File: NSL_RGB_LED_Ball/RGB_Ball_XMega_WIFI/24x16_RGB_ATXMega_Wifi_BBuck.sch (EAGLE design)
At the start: 107 parts, among them IC2 TLC5947XLP, IC3 TLC5947XLP, IC4 TLC5947XLP, IC5 MCP73123, IC6 CC3000, IC7 MMA7455L, IC8 OPA344, X1 NX3225GA-16.000M-STD-CRG-2

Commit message: 
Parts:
- removed BATTERY1: (no value), SparkFun:M02PTH
- added C26, C28, C30: 10uF, CH_passive:CAP0805
- added C27, C29: 0.1, CH_passive:CAP0805
- added L3: 2.2uH 1.6A, CH_passive:INDUCTOR1313
- added R16, R9: see notes, CH_passive:RESISTOR0805
- added R17: 100K, slice_noshift:RESISTOR0805
- added R7, R8: 1M, CH_passive:RESISTOR0805
- added U1: TPS6120x, CH_TI:TPS61200
- R6: value 220K -> 100K
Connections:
- new net +3V3: C1.1, C2.1, C20.2, C28.1, C30.1, C5.1, C6.1, C7.1, C8.1, IC1.AVCC, IC1.VCC@1, IC1.VCC@2, IC1.VCC@3, IC7.AVDD, IC7.DVDD_IO, IC8.V+, JP1.4, R11.2, R13.2, U1.FB, U1.VOUT, Z1.P$4
- new net EN: R7.1, U1.EN
- new net N$24: L3.2, U1.L
- new net N$30: C27.1, U1.VAUX
- new net PS: R8.1, U1.PS
- new net UVLO: C29.2, R16.2, R9.1, U1.UVLO
- net BATTSENSE: now also R17.2
- net GND: now also C26.2, C27.2, C28.2, C30.2, JP2.1, R16.1, R17.1, U1.GND, U1.PAD@1, U1.PAD@2, U1.PAD@3, U1.PAD@4, U1.PAD@5, U1.PGND; no longer BATTERY1.1, JP2.4, VCC.1
- net N$7: now also JP2.4; no longer JP2.1
- net VCC: now also C26.1, C29.1, L3.1, R7.2, R8.2, R9.2, U1.VIN, VCC.1; no longer BATTERY1.2, C1.1, C2.1, C20.2, C5.1, C6.1, C7.1, C8.1, IC1.AVCC, IC1.VCC@1, IC1.VCC@2, IC1.VCC@3, IC7.AVDD, IC7.DVDD_IO, IC8.V+, JP1.4, R11.2, R13.2, Z1.P$4
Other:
- note added: "GND, PGND connected w/non-current bearing trace"
- note added: "Notes:"
- note added: "R3 1330K, R4 249K"
- note added: "R3 2100K, R4 232K"
- note added: "R3 2150K, R4 249K"
- note added: "R3 549K, R4 249K"
- note added: "R3 953K,"
- note added: "R3, R4 1% film"
- note added: "R4 95.3K"
- note added: "Sumida CDRH2D18"
- note added: "UVLO 0.8V (Single NiMH)"
- note added: "UVLO 1.6V (Dual NiMH)"
- note added: "UVLO 2.4V (Triple NiMH)"
- note added: "UVLO 2.5V (LiPo)"
- note added: "UVLO 2.75V"
- note added: "UVLO 2.75V (LiPo)"
- note added: "same values can be used for 5V feedback divider"

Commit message: 
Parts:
- added C31: 12pF, SparkFun:CAP0805
- added C32: 1uF, 24x16_RGB:CAP0805
- added TP15: MIC, testpad:PTR1TP12SQ
- added TP16: BATT, testpad:PTR1TP12SQ
- C23: value .1uF -> 47uF; device SparkFun:CAP0805 -> slice_noshift:CAP_POL3528; MPN 08055C105MAT2A -> (none); OC_NEWARK 73T5385 -> unknown
- JP4: device SparkFun-Connectors:M041.27MM -> SparkFun-Connectors:M04PTH
- R1, R2, R3: value 47K -> 20K
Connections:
- net +3V3: now also C23.+, C31.1, C32.1
- net BATTSENSE: now also TP16.TP
- net GND: now also C23.-, C31.2, C32.2; no longer C23.2
- net MIC: now also TP15.TP
- net N$17: no longer C23.1
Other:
- note removed: "If making new board flip PWR and GND"
- moved on the sheet: C13

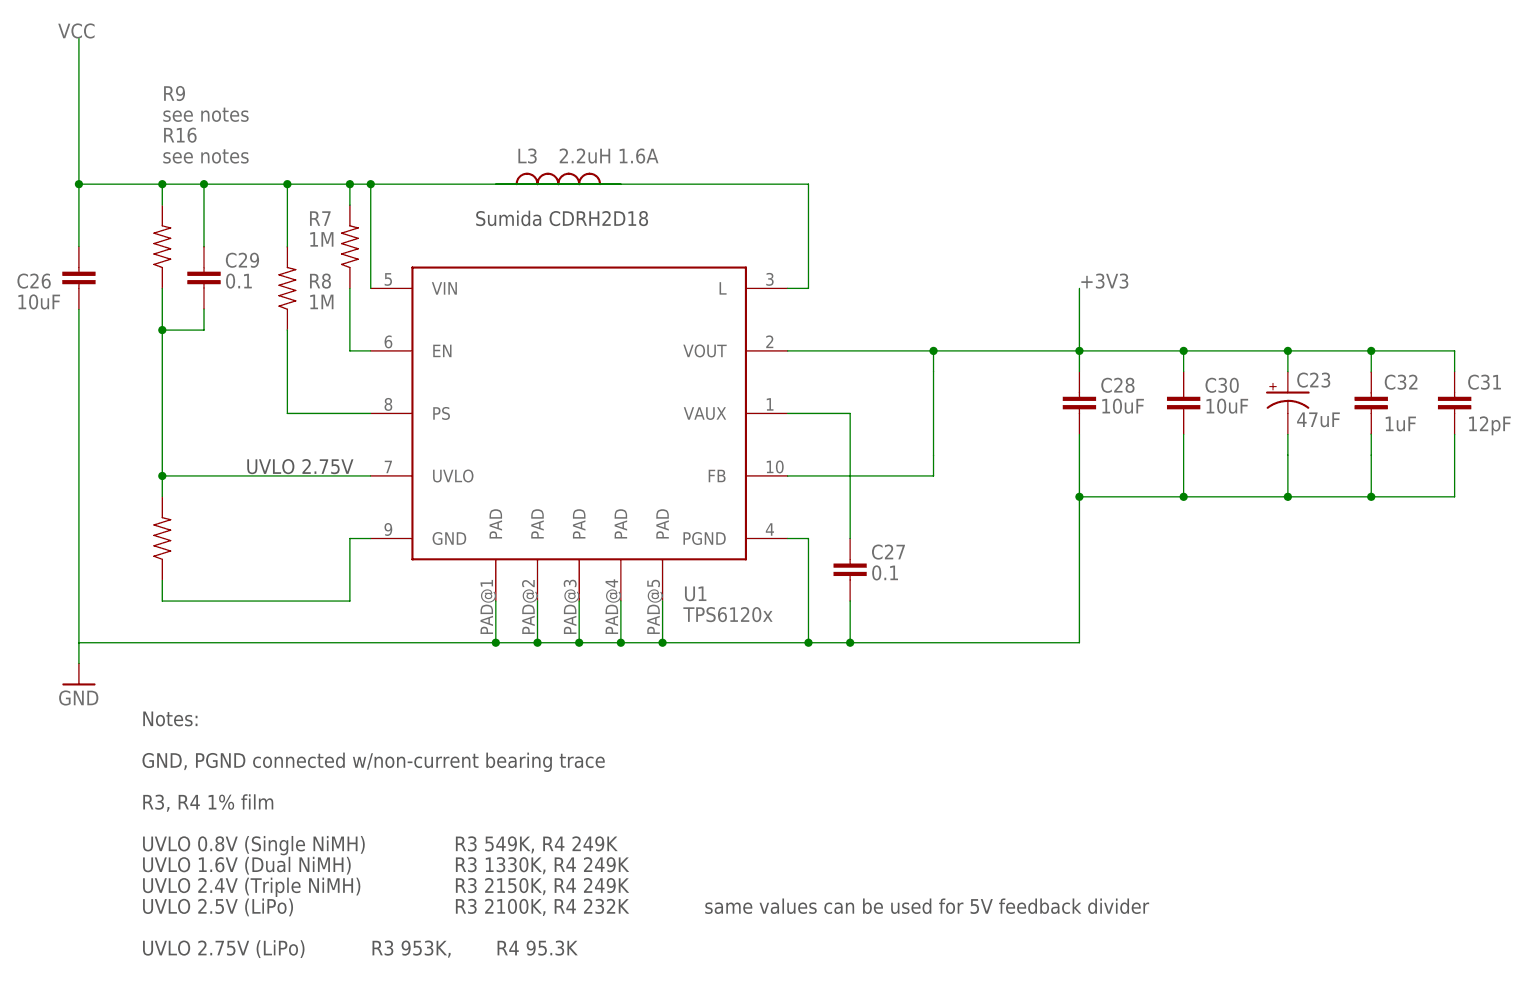
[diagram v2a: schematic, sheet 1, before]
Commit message: Changed to Buck Boost
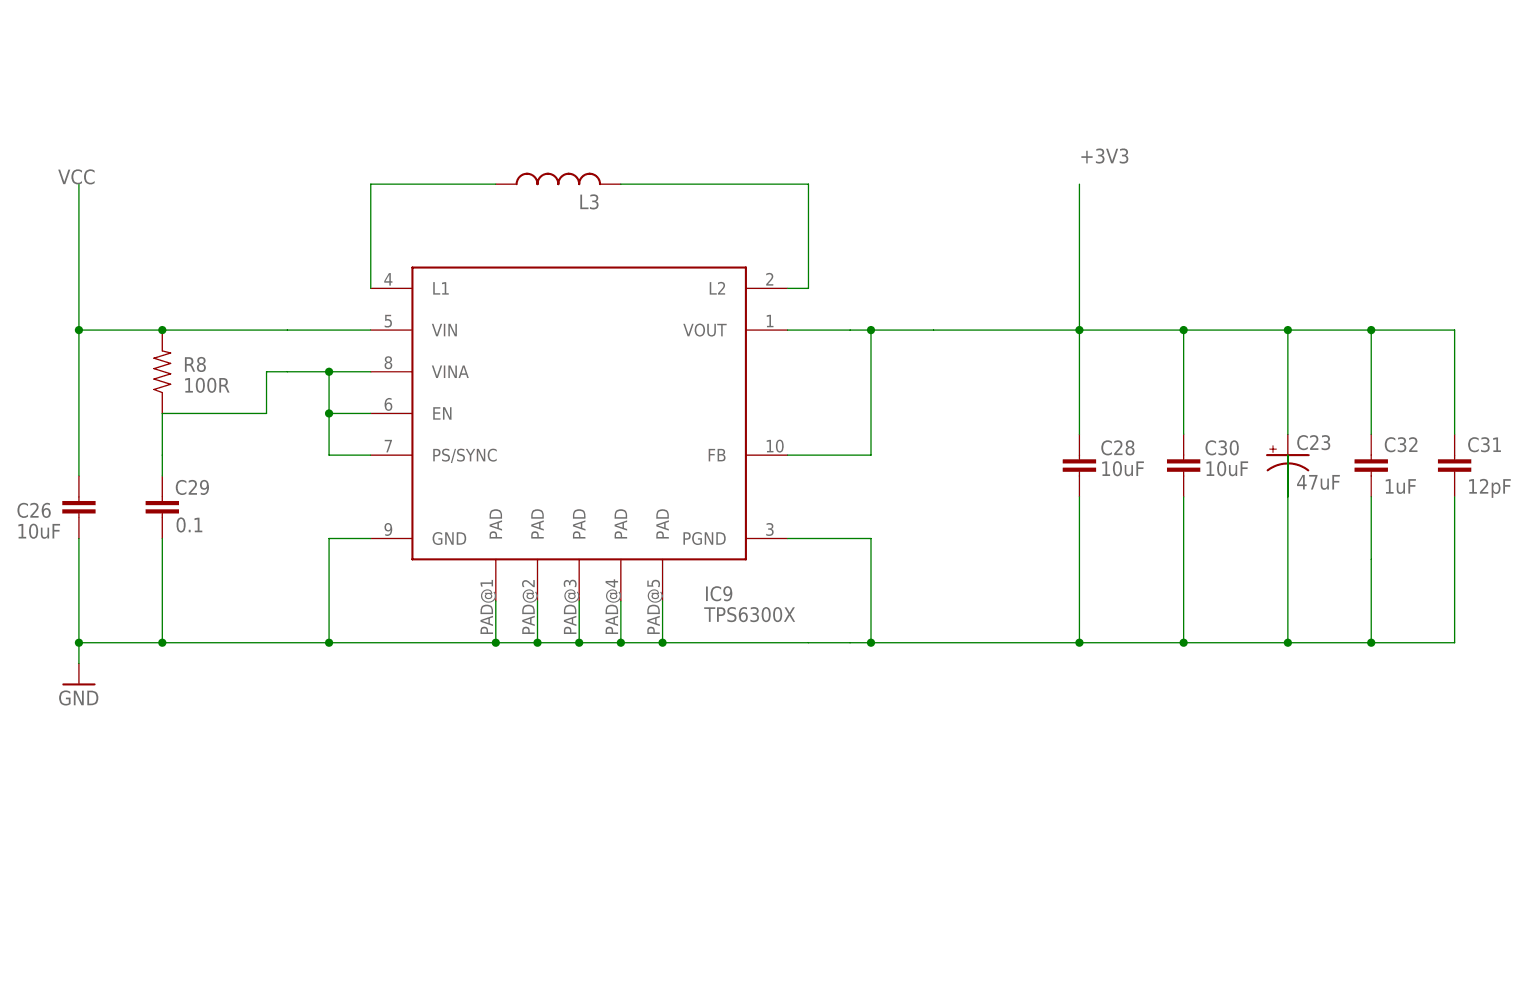
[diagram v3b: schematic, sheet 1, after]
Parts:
- removed C27: 0.1, CH_passive:CAP0805
- removed R16, R9: see notes, CH_passive:RESISTOR0805
- removed R7: 1M, CH_passive:RESISTOR0805
- removed U1: TPS6120x, CH_TI:TPS61200
- added IC9: TPS6300X, 24x16_RGB_ATXMega_Wifi_BBuck:TPS6300X
- L3: value 2.2uH 1.6A -> (none); device CH_passive:INDUCTOR1313 -> rcl:L-USL1812
- R8: value 1M -> 100R
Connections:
- removed net EN: R7.1, U1.EN
- removed net PS: R8.1, U1.PS
- removed net UVLO: C29.2, R16.2, R9.1, U1.UVLO
- new net N$32: C29.2, IC9.EN, IC9.PS/SYNC, IC9.VINA, R8.1
- net +3V3: now also IC9.FB, IC9.VOUT; no longer U1.FB, U1.VOUT
- net GND: now also C29.1, IC9.GND, IC9.PAD@1, IC9.PAD@2, IC9.PAD@3, IC9.PAD@4, IC9.PAD@5, IC9.PGND; no longer C27.2, R16.1, U1.GND, U1.PAD@1, U1.PAD@2, U1.PAD@3, U1.PAD@4, U1.PAD@5, U1.PGND
- net N$24: now also IC9.L2; no longer U1.L
- net N$30: now also IC9.L1, L3.1; no longer C27.1, U1.VAUX
- net VCC: now also IC9.VIN; no longer C29.1, L3.1, R7.2, R9.2, U1.VIN
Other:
- note removed: "GND, PGND connected w/non-current bearing trace"
- note removed: "Notes:"
- note removed: "R3 1330K, R4 249K"
- note removed: "R3 2100K, R4 232K"
- note removed: "R3 2150K, R4 249K"
- note removed: "R3 549K, R4 249K"
- note removed: "R3 953K,"
- note removed: "R3, R4 1% film"
- note removed: "R4 95.3K"
- note removed: "Sumida CDRH2D18"
- note removed: "UVLO 0.8V (Single NiMH)"
- note removed: "UVLO 1.6V (Dual NiMH)"
- note removed: "UVLO 2.4V (Triple NiMH)"
- note removed: "UVLO 2.5V (LiPo)"
- note removed: "UVLO 2.75V"
- note removed: "UVLO 2.75V (LiPo)"
- note removed: "same values can be used for 5V feedback divider"
- moved on the sheet: C23, C26, C28, C29, C30, C31, C32, R8

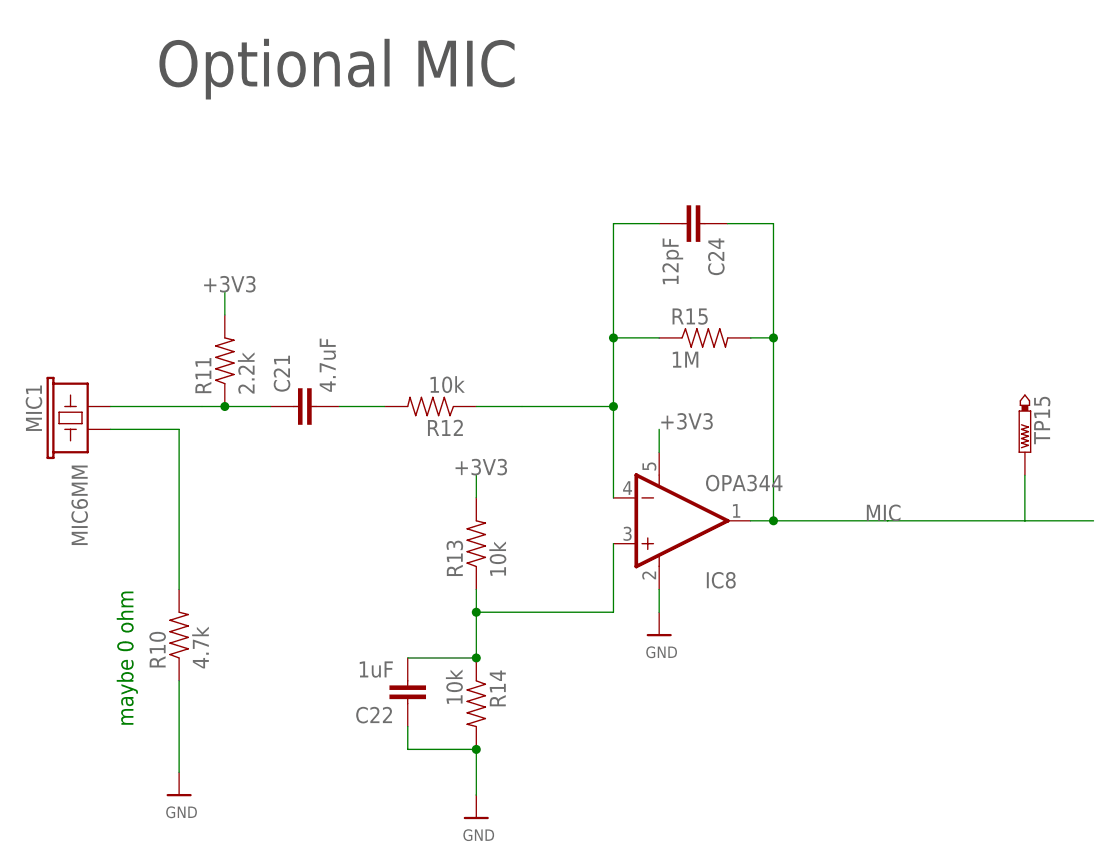
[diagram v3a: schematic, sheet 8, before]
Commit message: 
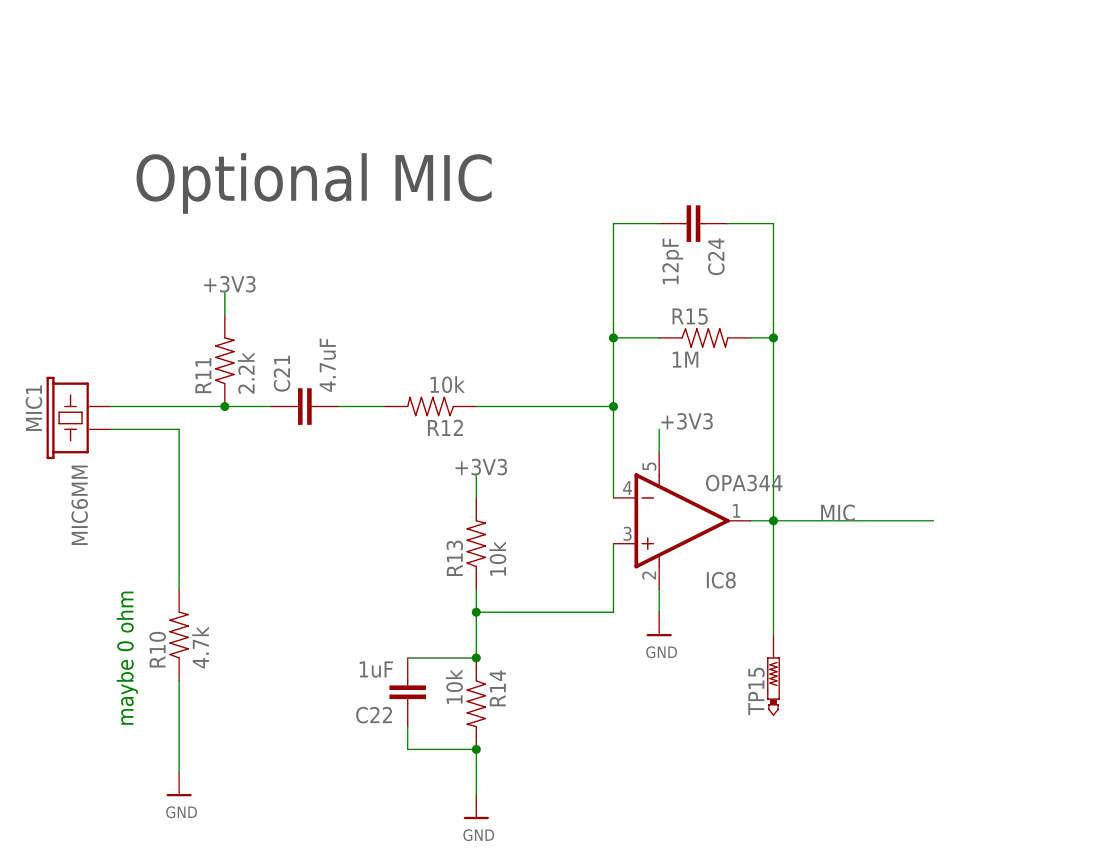
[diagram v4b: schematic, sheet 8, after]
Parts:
- removed JP2: (no value), SparkFun-Connectors:M041.27MM
- added JP5: (no value), SparkFun-Connectors:M04PTH
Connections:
- net D+: now also JP5.2; no longer JP2.2
- net D-: now also JP5.3; no longer JP2.3
- net GND: now also JP5.1; no longer JP2.1
- net N$7: now also JP5.4; no longer JP2.4
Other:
- moved on the sheet: TP15
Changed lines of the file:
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@@
 <part name="GND13" library="SparkFun" deviceset="GND" device=""/>
 <part name="D1" library="diode" deviceset="DIODE-" device="DO214AA" value="SSB44-E3/52T"/>
-<part name="JP2" library="SparkFun-Connectors" deviceset="M04" device="1.27MM"/>
 <part name="IC6" library="centerblack_engineering" deviceset="CC3000" device=""/>
 <part name="GND17" library="supply1" deviceset="GND" device=""/>
@@
 <part name="IC9" library="24x16_RGB_ATXMega_Wifi_BBuck" deviceset="TPS6300X" device=""/>
 <part name="L3" library="rcl" deviceset="L-US" device="L1812"/>
+<part name="JP5" library="SparkFun-Connectors" deviceset="M04" device="PTH"/>
 </parts>
 <sheets>
@@
 <instance part="GND12" gate="1" x="128.27" y="-48.26"/>
 <instance part="D1" gate="G$1" x="123.19" y="-41.91" rot="R180"/>
-<instance part="JP2" gate="G$1" x="119.38" y="-22.86"/>
 <instance part="GND20" gate="1" x="-69.85" y="-58.42"/>
 <instance part="Z1" gate="G$1" x="88.9" y="-33.02" rot="MR0"/>
 <instance part="GND32" gate="1" x="93.98" y="-48.26"/>
 <instance part="JP4" gate="G$1" x="-76.2" y="-49.53"/>
+<instance part="JP5" gate="G$1" x="116.332" y="-22.86"/>
 </instances>
 <busses>
@@
 </segment>
 <segment>
-<wire x1="134.62" y1="-25.4" x2="124.46" y2="-25.4" width="0.1524" layer="91"/>
-<pinref part="JP2" gate="G$1" pin="1"/>
+<wire x1="134.62" y1="-25.4" x2="121.412" y2="-25.4" width="0.1524" layer="91"/>
 <label x="129.54" y="-25.4" size="1.778" layer="95"/>
+<pinref part="JP5" gate="G$1" pin="1"/>
 </segment>
 </net>
@@
 </segment>
 <segment>
-<wire x1="124.46" y1="-20.32" x2="134.62" y2="-20.32" width="0.1524" layer="91"/>
+<wire x1="121.412" y1="-20.32" x2="134.62" y2="-20.32" width="0.1524" layer="91"/>
 <label x="129.54" y="-20.32" size="1.778" layer="95"/>
-<pinref part="JP2" gate="G$1" pin="3"/>
+<pinref part="JP5" gate="G$1" pin="3"/>
 </segment>
 <segment>
@@
 </segment>
 <segment>
-<wire x1="124.46" y1="-22.86" x2="134.62" y2="-22.86" width="0.1524" layer="91"/>
-<pinref part="JP2" gate="G$1" pin="2"/>
+<wire x1="121.412" y1="-22.86" x2="134.62" y2="-22.86" width="0.1524" layer="91"/>
 <label x="129.54" y="-22.86" size="1.778" layer="95"/>
+<pinref part="JP5" gate="G$1" pin="2"/>
 </segment>
 <segment>
@@
 </segment>
 <segment>
-<wire x1="134.62" y1="-17.78" x2="124.46" y2="-17.78" width="0.1524" layer="91"/>
+<wire x1="134.62" y1="-17.78" x2="121.412" y2="-17.78" width="0.1524" layer="91"/>
 <label x="129.54" y="-17.78" size="1.778" layer="95"/>
-<pinref part="JP2" gate="G$1" pin="4"/>
+<pinref part="JP5" gate="G$1" pin="4"/>
 </segment>
 </net>
@@
 <sheet>
 <plain>
-<text x="-54.61" y="64.77" size="12.7" layer="97">WiFi CC3000</text>
+<text x="-82.55" y="19.05" size="12.7" layer="97">WiFi CC3000</text>
 </plain>
 <instances>
@@
 </segment>
 </net>
-<net name="BT_RST" class="0">
-<segment>
-<wire x1="-193.04" y1="-5.08" x2="-200.66" y2="-5.08" width="0.1524" layer="91"/>
-<label x="-200.66" y="-5.08" size="1.778" layer="95"/>
-</segment>
-</net>
 <net name="WL_EN1" class="0">
 <segment>
@@
 <sheet>
 <plain>
-<text x="-35.56" y="50.8" size="5.08" layer="97" font="vector">Optional MIC</text>
+<text x="-38.1" y="38.1" size="5.08" layer="97" font="vector">Optional MIC</text>
 <text x="-38.1" y="-20.32" size="1.778" layer="91" rot="R90">maybe 0 ohm</text>
 </plain>
@@
 </instance>
 <instance part="U$1" gate="G$1" x="-33.02" y="-27.94"/>
-<instance part="TP15" gate="G$1" x="60.96" y="10.16" rot="R180"/>
+<instance part="TP15" gate="G$1" x="33.02" y="-12.7"/>
 </instances>
 <busses>
@@
 <segment>
 <wire x1="27.94" y1="35.56" x2="33.02" y2="35.56" width="0.1524" layer="91"/>
-<wire x1="33.02" y1="2.54" x2="45.72" y2="2.54" width="0.1524" layer="91"/>
 <wire x1="30.48" y1="22.86" x2="33.02" y2="22.86" width="0.1524" layer="91"/>
 <wire x1="33.02" y1="22.86" x2="33.02" y2="2.54" width="0.1524" layer="91"/>
 <wire x1="30.48" y1="2.54" x2="33.02" y2="2.54" width="0.1524" layer="91"/>
 <wire x1="33.02" y1="35.56" x2="33.02" y2="22.86" width="0.1524" layer="91"/>
-<label x="43.18" y="2.54" size="1.778" layer="95"/>
+<label x="38.1" y="2.54" size="1.778" layer="95"/>
 <pinref part="C24" gate="G$1" pin="1"/>
 <pinref part="R15" gate="G$1" pin="2"/>
@@
 <junction x="33.02" y="22.86"/>
 <junction x="33.02" y="2.54"/>
-<wire x1="45.72" y1="2.54" x2="60.96" y2="2.54" width="0.1524" layer="91"/>
 <pinref part="TP15" gate="G$1" pin="TP"/>
-<wire x1="60.96" y1="2.54" x2="68.58" y2="2.54" width="0.1524" layer="91"/>
-<wire x1="60.96" y1="2.54" x2="60.96" y2="7.62" width="0.1524" layer="91"/>
+<wire x1="33.02" y1="2.54" x2="50.8" y2="2.54" width="0.1524" layer="91"/>
+<wire x1="33.02" y1="2.54" x2="33.02" y2="-10.16" width="0.1524" layer="91"/>
 </segment>
 </net>
